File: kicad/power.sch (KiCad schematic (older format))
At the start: 30 parts, among them CON23 PS-ON, CON24 CON6, CON25 FAN, CON26 Chamber, Q7 FDC6401N, Q8 FDC6401N, Q9 FDC6401N

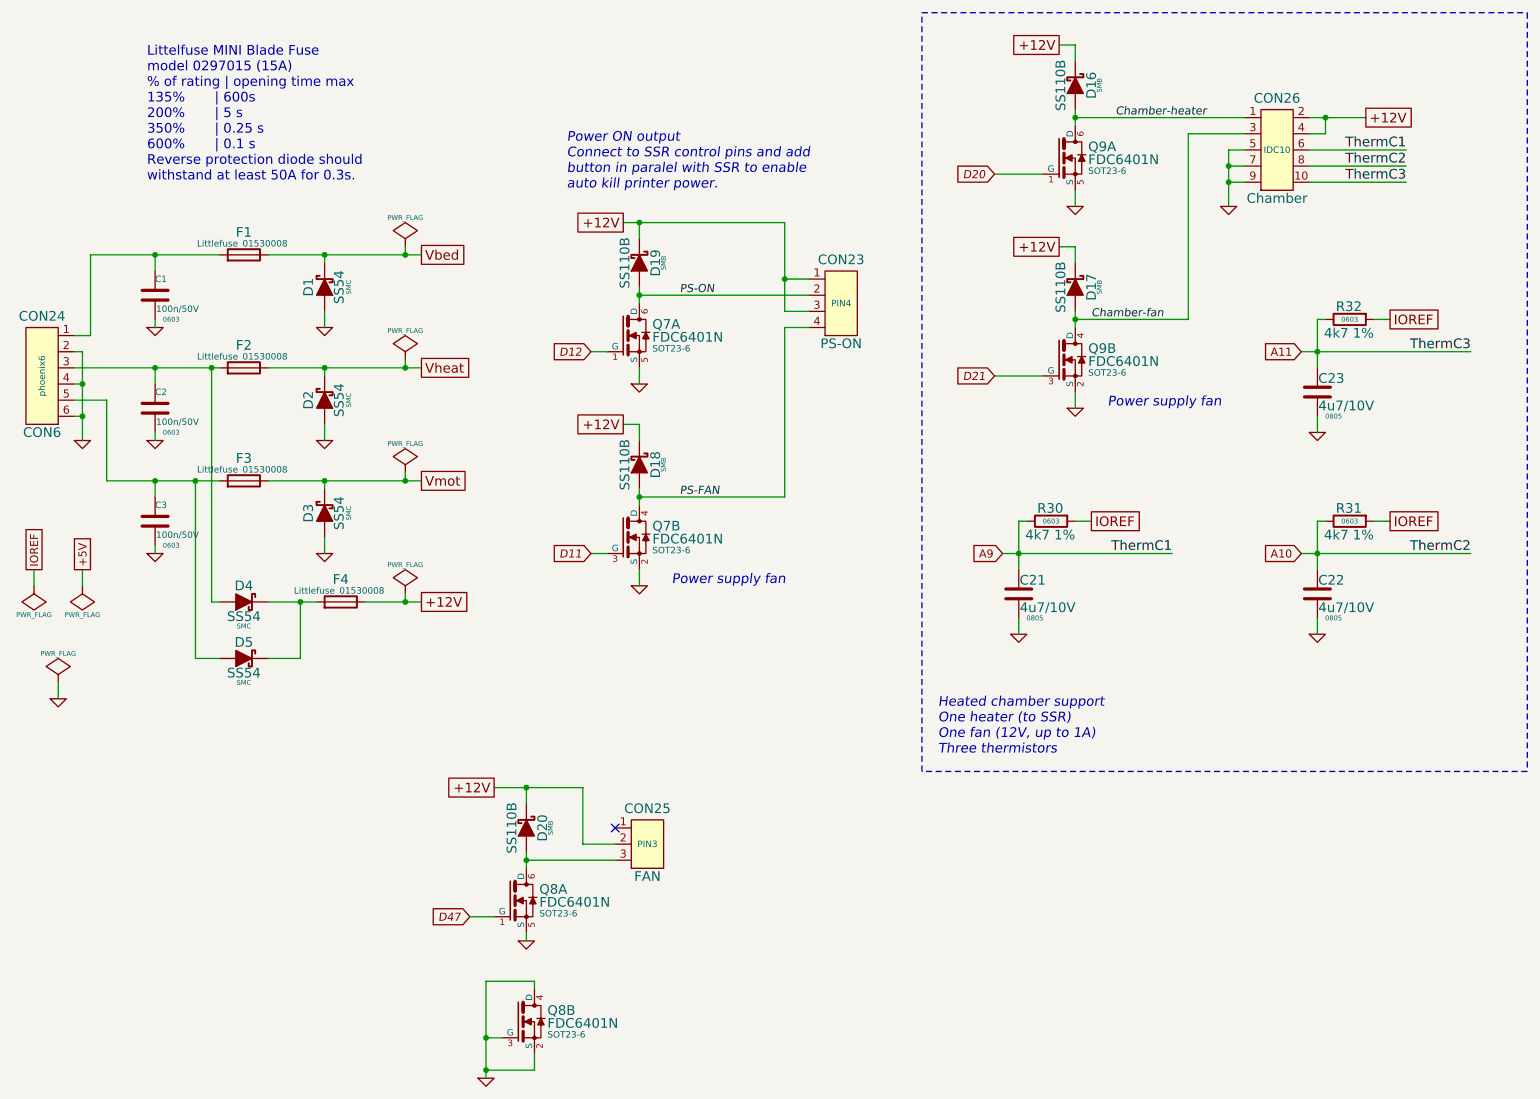
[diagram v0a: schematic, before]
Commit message: Change 1A diodes. Add capacitors next to OC outputs. Place.
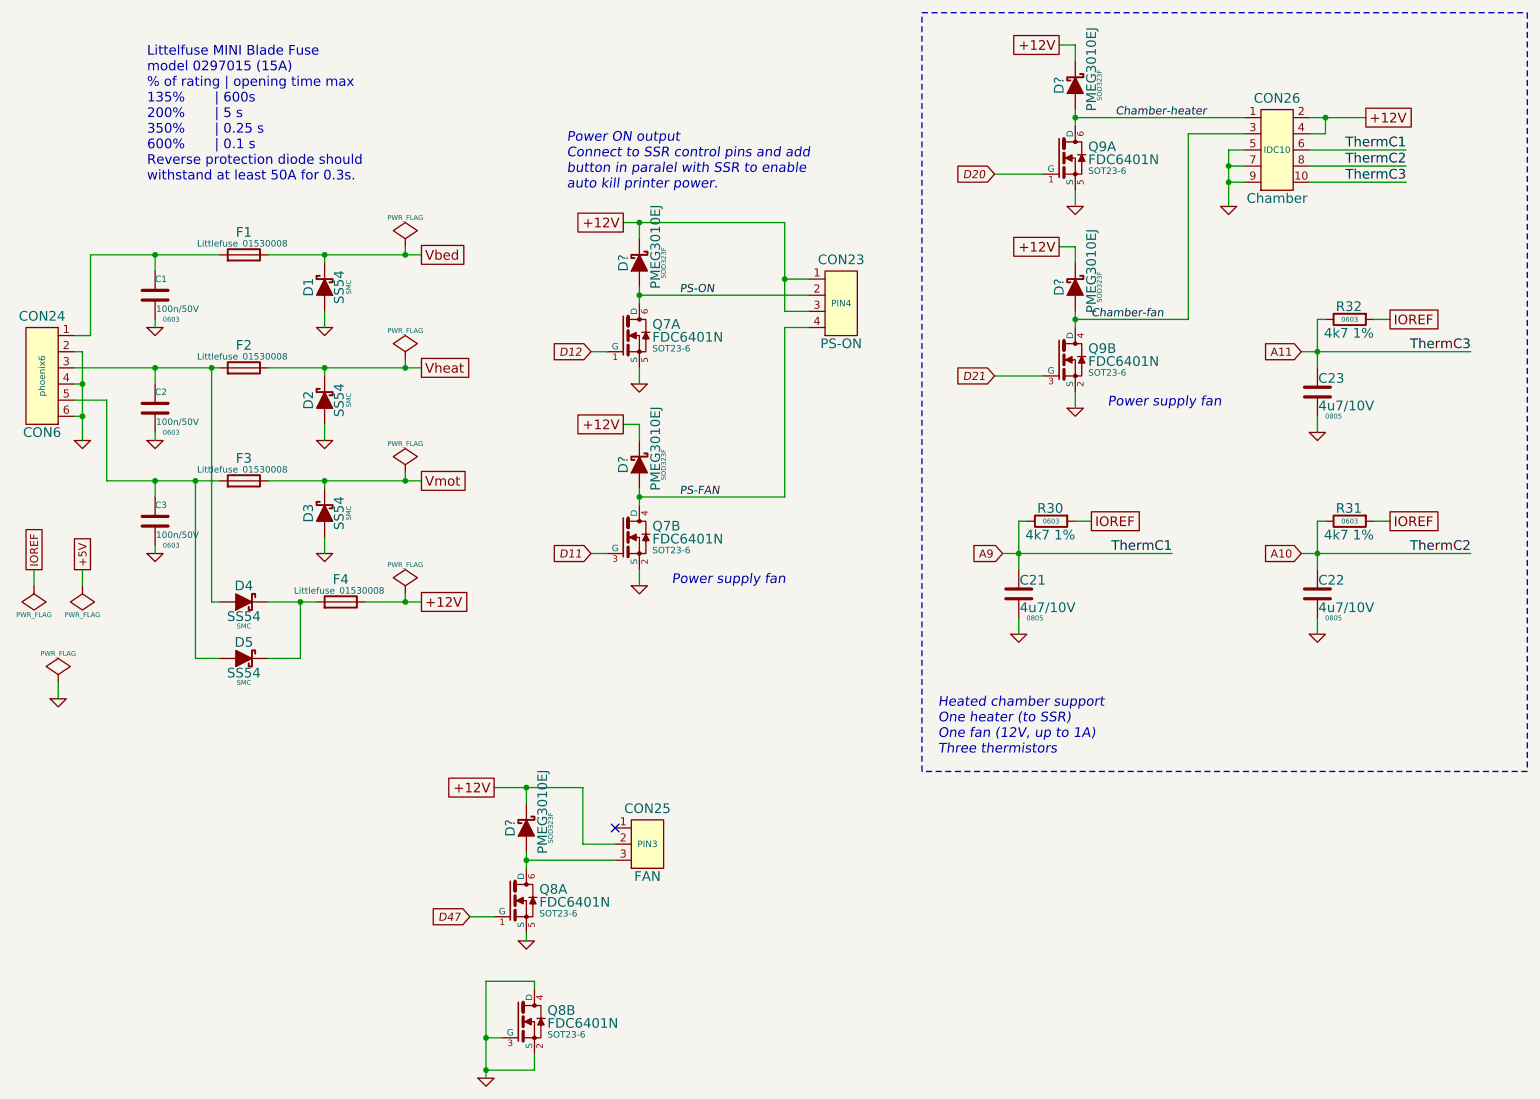
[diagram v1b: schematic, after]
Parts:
- removed D16, D17, D18, D19, D20: SS110B, SMB, symbol SS110B
- added D? (x5): PMEG3010EJ, SOD323F, symbol PMEG3010EJ
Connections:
- net +12V: now also D?.1, D?.1, D?.1, D?.1, D?.1
- net Chamber-fan: now also D?.2
- net Chamber-heater: now also D?.2
- net PS-FAN: now also D?.2
- net PS-ON: now also D?.2
- net at CON25.3, Q8.6 (D): now also D?.2
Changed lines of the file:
@@
 	1    0    0    -1
-$EndComp
-$Comp
-L SS110B D19
-U 1 1 53949E2B
-P 4850 2150
-F 0 "D19" H 4850 2050 60  0000 C CNN
-F 1 "SS110B" H 4850 2240 60  0000 C CNN
-F 2 "SMB" H 4850 2000 30  0000 C CNN
-F 3 "" V 4850 2150 60  0000 C CNN
-	1    4850 2150
-	0    -1   -1   0
 $EndComp
 Wire Wire Line
@@
 Heated chamber support\nOne heater (to SSR)\nOne fan (12V, up to 1A)\nThree thermistors
 $Comp
-L SS110B D18
-U 1 1 539B1F63
+L PMEG3010EJ D?
+U 1 1 539CBBDC
 P 4850 3400
-F 0 "D18" H 4850 3300 60  0000 C CNN
-F 1 "SS110B" H 4850 3490 60  0000 C CNN
-F 2 "SMB" H 4850 3250 30  0000 C CNN
+F 0 "D?" H 4850 3500 60  0000 C CNN
+F 1 "PMEG3010EJ" H 4950 3300 60  0000 C CNN
+F 2 "SOD323F" H 4850 3250 30  0000 C CNN
 F 3 "" V 4850 3400 60  0000 C CNN
 	1    4850 3400
@@
 $EndComp
 $Comp
-L SS110B D17
-U 1 1 539B1FBA
+L PMEG3010EJ D?
+U 1 1 539CBCF5
+P 4850 2150
+F 0 "D?" H 4850 2250 60  0000 C CNN
+F 1 "PMEG3010EJ" H 4950 2050 60  0000 C CNN
+F 2 "SOD323F" H 4850 2000 30  0000 C CNN
+F 3 "" V 4850 2150 60  0000 C CNN
+	1    4850 2150
+	0    -1   -1   0
+$EndComp
+$Comp
+L PMEG3010EJ D?
+U 1 1 539CBD53
+P 7550 1050
+F 0 "D?" H 7550 1150 60  0000 C CNN
+F 1 "PMEG3010EJ" H 7650 950 60  0000 C CNN
+F 2 "SOD323F" H 7550 900 30  0000 C CNN
+F 3 "" V 7550 1050 60  0000 C CNN
+	1    7550 1050
+	0    -1   -1   0
+$EndComp
+$Comp
+L PMEG3010EJ D?
+U 1 1 539CBDBC
 P 7550 2300
-F 0 "D17" H 7550 2200 60  0000 C CNN
-F 1 "SS110B" H 7550 2390 60  0000 C CNN
-F 2 "SMB" H 7550 2150 30  0000 C CNN
+F 0 "D?" H 7550 2400 60  0000 C CNN
+F 1 "PMEG3010EJ" H 7650 2200 60  0000 C CNN
+F 2 "SOD323F" H 7550 2150 30  0000 C CNN
 F 3 "" V 7550 2300 60  0000 C CNN
 	1    7550 2300
@@
 $EndComp
 $Comp
-L SS110B D16
-U 1 1 539B202A
-P 7550 1050
-F 0 "D16" H 7550 950 60  0000 C CNN
-F 1 "SS110B" H 7550 1140 60  0000 C CNN
-F 2 "SMB" H 7550 900 30  0000 C CNN
-F 3 "" V 7550 1050 60  0000 C CNN
-	1    7550 1050
-	0    -1   -1   0
-$EndComp
-$Comp
-L SS110B D20
-U 1 1 539B228F
+L PMEG3010EJ D?
+U 1 1 539CBE38
 P 4150 5650
-F 0 "D20" H 4150 5550 60  0000 C CNN
-F 1 "SS110B" H 4150 5740 60  0000 C CNN
-F 2 "SMB" H 4150 5500 30  0000 C CNN
+F 0 "D?" H 4150 5750 60  0000 C CNN
+F 1 "PMEG3010EJ" H 4250 5550 60  0000 C CNN
+F 2 "SOD323F" H 4150 5500 30  0000 C CNN
 F 3 "" V 4150 5650 60  0000 C CNN
 	1    4150 5650

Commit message: Place
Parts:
- added C27, C28, C29: 100n/50V, 0603, symbol C
- gave numbers to parts that had none: 5
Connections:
- net +12V: now also C27.1, C28.1, C29.1
- net GND: now also C27.2, C28.2, C29.2

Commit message: Fix panel connections. Place.
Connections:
- net D11: now also Q7.1 (G); no longer Q7.3 (G)
- net D12: now also Q7.3 (G); no longer Q7.1 (G)
- net PS-FAN: now also Q7.6 (D); no longer Q7.4 (D)
- net PS-ON: now also Q7.4 (D); no longer Q7.6 (D)
- net D20 renamed A3
- net D21 renamed A4
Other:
- moved on the sheet: Q7A, Q7B
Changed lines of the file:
@@
 $EndDescr
 $Comp
-L GND #PWR68
+L GND #PWR060
 U 1 1 53943822
 P 1400 3250
-F 0 "#PWR68" H 1400 3250 30  0001 C CNN
+F 0 "#PWR060" H 1400 3250 30  0001 C CNN
 F 1 "GND" H 1400 3180 30  0001 C CNN
 F 2 "" H 1400 3250 60  0000 C CNN
@@
 Littelfuse MINI Blade Fuse\nmodel 0297015 (15A)\n% of rating | opening time max\n135%       | 600s\n200%       | 5 s \n350%       | 0.25 s \n600%       | 0.1 s\nReverse protection diode should \nwithstand at least 50A for 0.3s.
 $Comp
-L GND #PWR70
+L GND #PWR061
 U 1 1 53943829
 P 2900 3250
-F 0 "#PWR70" H 2900 3250 30  0001 C CNN
+F 0 "#PWR061" H 2900 3250 30  0001 C CNN
 F 1 "GND" H 2900 3180 30  0001 C CNN
 F 2 "" H 2900 3250 60  0000 C CNN
@@
 $EndComp
 $Comp
-L GND #PWR64
+L GND #PWR062
 U 1 1 5394382F
 P 2900 2550
-F 0 "#PWR64" H 2900 2550 30  0001 C CNN
+F 0 "#PWR062" H 2900 2550 30  0001 C CNN
 F 1 "GND" H 2900 2480 30  0001 C CNN
 F 2 "" H 2900 2550 60  0000 C CNN
@@
 $EndComp
 $Comp
-L GND #PWR73
+L GND #PWR063
 U 1 1 53943835
 P 2900 3950
-F 0 "#PWR73" H 2900 3950 30  0001 C CNN
+F 0 "#PWR063" H 2900 3950 30  0001 C CNN
 F 1 "GND" H 2900 3880 30  0001 C CNN
 F 2 "" H 2900 3950 60  0000 C CNN
@@
 $EndComp
 $Comp
-L GND #PWR63
+L GND #PWR064
 U 1 1 53943842
 P 1850 2550
-F 0 "#PWR63" H 1850 2550 30  0001 C CNN
+F 0 "#PWR064" H 1850 2550 30  0001 C CNN
 F 1 "GND" H 1850 2480 30  0001 C CNN
 F 2 "" H 1850 2550 60  0000 C CNN
@@
 $EndComp
 $Comp
-L GND #PWR69
+L GND #PWR065
 U 1 1 53943848
 P 1850 3250
-F 0 "#PWR69" H 1850 3250 30  0001 C CNN
+F 0 "#PWR065" H 1850 3250 30  0001 C CNN
 F 1 "GND" H 1850 3180 30  0001 C CNN
 F 2 "" H 1850 3250 60  0000 C CNN
@@
 $EndComp
 $Comp
-L GND #PWR72
+L GND #PWR066
 U 1 1 5394384E
 P 1850 3950
-F 0 "#PWR72" H 1850 3950 30  0001 C CNN
+F 0 "#PWR066" H 1850 3950 30  0001 C CNN
 F 1 "GND" H 1850 3880 30  0001 C CNN
 F 2 "" H 1850 3950 60  0000 C CNN
@@
 $EndComp
 $Comp
-L PWR_FLAG #FLG1
+L PWR_FLAG #FLG067
 U 1 1 539438AC
 P 3400 2050
-F 0 "#FLG1" H 3400 2145 30  0001 C CNN
+F 0 "#FLG067" H 3400 2145 30  0001 C CNN
 F 1 "PWR_FLAG" H 3400 2230 30  0000 C CNN
 F 2 "" H 3400 2050 60  0000 C CNN
@@
 $EndComp
 $Comp
-L PWR_FLAG #FLG2
+L PWR_FLAG #FLG068
 U 1 1 539438B2
 P 3400 2750
-F 0 "#FLG2" H 3400 2845 30  0001 C CNN
+F 0 "#FLG068" H 3400 2845 30  0001 C CNN
 F 1 "PWR_FLAG" H 3400 2930 30  0000 C CNN
 F 2 "" H 3400 2750 60  0000 C CNN
@@
 $EndComp
 $Comp
-L PWR_FLAG #FLG3
+L PWR_FLAG #FLG069
 U 1 1 539438B8
 P 3400 3450
-F 0 "#FLG3" H 3400 3545 30  0001 C CNN
+F 0 "#FLG069" H 3400 3545 30  0001 C CNN
 F 1 "PWR_FLAG" H 3400 3630 30  0000 C CNN
 F 2 "" H 3400 3450 60  0000 C CNN
@@
 $EndComp
 $Comp
-L PWR_FLAG #FLG6
+L PWR_FLAG #FLG070
 U 1 1 539438BE
 P 3400 4200
-F 0 "#FLG6" H 3400 4295 30  0001 C CNN
+F 0 "#FLG070" H 3400 4295 30  0001 C CNN
 F 1 "PWR_FLAG" H 3400 4380 30  0000 C CNN
 F 2 "" H 3400 4200 60  0000 C CNN
@@
 $EndComp
 $Comp
-L PWR_FLAG #FLG7
+L PWR_FLAG #FLG071
 U 1 1 539438C4
 P 1250 4750
-F 0 "#FLG7" H 1250 4845 30  0001 C CNN
+F 0 "#FLG071" H 1250 4845 30  0001 C CNN
 F 1 "PWR_FLAG" H 1250 4930 30  0000 C CNN
 F 2 "" H 1250 4750 60  0000 C CNN
@@
 $EndComp
 $Comp
-L GND #PWR77
+L GND #PWR072
 U 1 1 539438CA
 P 1250 4850
-F 0 "#PWR77" H 1250 4850 30  0001 C CNN
+F 0 "#PWR072" H 1250 4850 30  0001 C CNN
 F 1 "GND" H 1250 4780 30  0001 C CNN
 F 2 "" H 1250 4850 60  0000 C CNN
@@
 IOREF
 $Comp
-L PWR_FLAG #FLG5
+L PWR_FLAG #FLG073
 U 1 1 53943908
 P 1400 4150
-F 0 "#FLG5" H 1400 4245 30  0001 C CNN
+F 0 "#FLG073" H 1400 4245 30  0001 C CNN
 F 1 "PWR_FLAG" H 1400 4330 30  0000 C CNN
 F 2 "" H 1400 4150 60  0000 C CNN
@@
 $EndComp
 $Comp
-L PWR_FLAG #FLG4
+L PWR_FLAG #FLG074
 U 1 1 5394390F
 P 1100 4150
-F 0 "#FLG4" H 1100 4245 30  0001 C CNN
+F 0 "#FLG074" H 1100 4245 30  0001 C CNN
 F 1 "PWR_FLAG" H 1100 4330 30  0000 C CNN
 F 2 "" H 1100 4150 60  0000 C CNN
@@
 L FDC6401N Q7
 U 1 1 5394391D
+P 4750 3850
+F 0 "Q7" H 4930 3920 60  0000 L CNN
+F 1 "FDC6401N" H 4930 3840 60  0000 L CNN
+F 2 "SOT23-6" H 4930 3770 40  0000 L CNN
+F 3 "" H 4750 3800 60  0000 C CNN
+	1    4750 3850
+	1    0    0    -1
+$EndComp
+$Comp
+L FDC6401N Q7
+U 2 1 53943924
 P 4750 2600
 F 0 "Q7" H 4930 2670 60  0000 L CNN
@@
 F 2 "SOT23-6" H 4930 2520 40  0000 L CNN
 F 3 "" H 4750 2550 60  0000 C CNN
-	1    4750 2600
-	1    0    0    -1
-$EndComp
-$Comp
-L FDC6401N Q7
-U 2 1 53943924
-P 4750 3850
-F 0 "Q7" H 4930 3920 60  0000 L CNN
-F 1 "FDC6401N" H 4930 3840 60  0000 L CNN
-F 2 "SOT23-6" H 4930 3770 40  0000 L CNN
-F 3 "" H 4750 3800 60  0000 C CNN
-	2    4750 3850
-	1    0    0    -1
-$EndComp
-$Comp
-L GND #PWR74
+	2    4750 2600
+	1    0    0    -1
+$EndComp
+$Comp
+L GND #PWR075
 U 1 1 53943ED6
 P 4850 4150
-F 0 "#PWR74" H 4850 4150 30  0001 C CNN
+F 0 "#PWR075" H 4850 4150 30  0001 C CNN
 F 1 "GND" H 4850 4080 30  0001 C CNN
 F 2 "" H 4850 4150 60  0000 C CNN
@@
 $EndComp
 $Comp
-L GND #PWR65
+L GND #PWR076
 U 1 1 53943F43
 P 4850 2900
-F 0 "#PWR65" H 4850 2900 30  0001 C CNN
+F 0 "#PWR076" H 4850 2900 30  0001 C CNN
 F 1 "GND" H 4850 2830 30  0001 C CNN
 F 2 "" H 4850 2900 60  0000 C CNN
@@
 D47
 $Comp
-L GND #PWR79
+L GND #PWR077
 U 1 1 53948CCE
 P 4150 6350
-F 0 "#PWR79" H 4150 6350 30  0001 C CNN
+F 0 "#PWR077" H 4150 6350 30  0001 C CNN
 F 1 "GND" H 4150 6280 30  0001 C CNN
 F 2 "" H 4150 6350 60  0000 C CNN
@@
 Connection ~ 3900 7150
 $Comp
-L GND #PWR80
+L GND #PWR078
 U 1 1 53949810
 P 3900 7200
-F 0 "#PWR80" H 3900 7200 30  0001 C CNN
+F 0 "#PWR078" H 3900 7200 30  0001 C CNN
 F 1 "GND" H 3900 7130 30  0001 C CNN
 F 2 "" H 3900 7200 60  0000 C CNN
@@
 $EndComp
 $Comp
-L GND #PWR66
+L GND #PWR079
 U 1 1 5394A1DE
 P 7550 3050
-F 0 "#PWR66" H 7550 3050 30  0001 C CNN
+F 0 "#PWR079" H 7550 3050 30  0001 C CNN
 F 1 "GND" H 7550 2980 30  0001 C CNN
 F 2 "" H 7550 3050 60  0000 C CNN
@@
 $EndComp
 $Comp
-L GND #PWR61
+L GND #PWR080
 U 1 1 5394A1E4
 P 7550 1800
-F 0 "#PWR61" H 7550 1800 30  0001 C CNN
+F 0 "#PWR080" H 7550 1800 30  0001 C CNN
 F 1 "GND" H 7550 1730 30  0001 C CNN
 F 2 "" H 7550 1800 60  0000 C CNN
@@
 +12V
 Text GLabel 7050 1600 0    50   Input Italic 0
-D20
+A3
 Wire Wire Line
 	7550 1200 7550 1300
@@
 	7350 2850 7050 2850
 Text GLabel 7050 2850 0    50   Input Italic 0
-D21
+A4
 Text Notes 7750 3050 0    60   Italic 0
 Power supply fan
@@
 Connection ~ 8500 1550
 $Comp
-L GND #PWR62
+L GND #PWR081
 U 1 1 5394B08E
 P 8500 1800
-F 0 "#PWR62" H 8500 1800 30  0001 C CNN
+F 0 "#PWR081" H 8500 1800 30  0001 C CNN
 F 1 "GND" H 8500 1730 30  0001 C CNN
 F 2 "" H 8500 1800 60  0000 C CNN
@@
 $EndComp
 $Comp
-L GND #PWR75
+L GND #PWR082
 U 1 1 5394B617
 P 7200 4450
-F 0 "#PWR75" H 7200 4450 30  0001 C CNN
+F 0 "#PWR082" H 7200 4450 30  0001 C CNN
 F 1 "GND" H 7200 4380 30  0001 C CNN
 F 2 "~" H 7200 4450 60  0000 C CNN
@@
 $EndComp
 $Comp
-L GND #PWR76
+L GND #PWR083
 U 1 1 5394B93D
 P 9050 4450
-F 0 "#PWR76" H 9050 4450 30  0001 C CNN
+F 0 "#PWR083" H 9050 4450 30  0001 C CNN
 F 1 "GND" H 9050 4380 30  0001 C CNN
 F 2 "~" H 9050 4450 60  0000 C CNN
@@
 $EndComp
 $Comp
-L GND #PWR67
+L GND #PWR084
 U 1 1 5394BA08
 P 9050 3200
-F 0 "#PWR67" H 9050 3200 30  0001 C CNN
+F 0 "#PWR084" H 9050 3200 30  0001 C CNN
 F 1 "GND" H 9050 3130 30  0001 C CNN
 F 2 "~" H 9050 3200 60  0000 C CNN
@@
 $EndComp
 $Comp
-L GND #PWR78
+L GND #PWR085
 U 1 1 539CFAEC
 P 3850 5850
-F 0 "#PWR78" H 3850 5850 30  0001 C CNN
+F 0 "#PWR085" H 3850 5850 30  0001 C CNN
 F 1 "GND" H 3850 5780 30  0001 C CNN
 F 2 "" H 3850 5850 60  0000 C CNN
@@
 $EndComp
 $Comp
-L GND #PWR71
+L GND #PWR086
 U 1 1 539CFEC7
 P 4500 3600
-F 0 "#PWR71" H 4500 3600 30  0001 C CNN
+F 0 "#PWR086" H 4500 3600 30  0001 C CNN
 F 1 "GND" H 4500 3530 30  0001 C CNN
 F 2 "" H 4500 3600 60  0000 C CNN
@@
 Connection ~ 7250 800
 $Comp
-L GND #PWR60
+L GND #PWR087
 U 1 1 539D0988
 P 7250 1250
-F 0 "#PWR60" H 7250 1250 30  0001 C CNN
+F 0 "#PWR087" H 7250 1250 30  0001 C CNN
 F 1 "GND" H 7250 1180 30  0001 C CNN
 F 2 "" H 7250 1250 60  0000 C CNN

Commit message: Delete fuse on +12V. Chcange fuse & diode placement.
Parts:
- removed F4: MINI_Blade_Fuse_Holder, Littlefuse_01530008, symbol MINI_Blade_Fuse_Holder
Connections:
- net +12V: now also D4.1, D5.1
- net Vheat: now also D4.2
- net Vmot: now also D5.2
- net at C2.1, CON24.3, F2.1: no longer D4.2
- net at C3.1, CON24.5, F3.1: no longer D5.2
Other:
- moved on the sheet: D4, D5, F2, F3
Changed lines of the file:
@@
 L SS54 D4
 U 1 1 5394387A
-P 2400 4250
-F 0 "D4" H 2400 4150 60  0000 C CNN
-F 1 "SS54" H 2400 4340 60  0000 C CNN
-F 2 "SMC" H 2400 4400 30  0000 C CNN
-F 3 "" V 2400 4250 60  0000 C CNN
-	1    2400 4250
+P 2900 4250
+F 0 "D4" H 2900 4150 60  0000 C CNN
+F 1 "SS54" H 2900 4340 60  0000 C CNN
+F 2 "SMC" H 2900 4400 30  0000 C CNN
+F 3 "" V 2900 4250 60  0000 C CNN
+	1    2900 4250
 	1    0    0    1
 $EndComp
@@
 L SS54 D5
 U 1 1 53943881
-P 2400 4600
-F 0 "D5" H 2400 4500 60  0000 C CNN
-F 1 "SS54" H 2400 4690 60  0000 C CNN
-F 2 "SMC" H 2400 4750 30  0000 C CNN
-F 3 "" V 2400 4600 60  0000 C CNN
-	1    2400 4600
+P 2900 4600
+F 0 "D5" H 2900 4500 60  0000 C CNN
+F 1 "SS54" H 2900 4690 60  0000 C CNN
+F 2 "SMC" H 2900 4750 30  0000 C CNN
+F 3 "" V 2900 4600 60  0000 C CNN
+	1    2900 4600
 	1    0    0    1
 $EndComp
@@
 L MINI_Blade_Fuse_Holder F2
 U 1 1 5394388F
-P 2400 2800
-F 0 "F2" H 2400 2940 60  0000 C CNN
-F 1 "MINI_Blade_Fuse_Holder" H 2400 2715 60  0001 C CNN
-F 2 "Littlefuse_01530008" H 2390 2870 40  0000 C CNN
-F 3 "" V 2400 2800 30  0000 C CNN
-	1    2400 2800
+P 2300 2800
+F 0 "F2" H 2300 2940 60  0000 C CNN
+F 1 "MINI_Blade_Fuse_Holder" H 2300 2715 60  0001 C CNN
+F 2 "Littlefuse_01530008" H 2290 2870 40  0000 C CNN
+F 3 "" V 2300 2800 30  0000 C CNN
+	1    2300 2800
 	1    0    0    -1
 $EndComp
@@
 L MINI_Blade_Fuse_Holder F3
 U 1 1 53943896
-P 2400 3500
-F 0 "F3" H 2400 3640 60  0000 C CNN
-F 1 "MINI_Blade_Fuse_Holder" H 2400 3415 60  0001 C CNN
-F 2 "Littlefuse_01530008" H 2390 3570 40  0000 C CNN
-F 3 "" V 2400 3500 30  0000 C CNN
-	1    2400 3500
-	1    0    0    -1
-$EndComp
-$Comp
-L MINI_Blade_Fuse_Holder F4
-U 1 1 5394389D
-P 3000 4250
-F 0 "F4" H 3000 4390 60  0000 C CNN
-F 1 "MINI_Blade_Fuse_Holder" H 3000 4165 60  0001 C CNN
-F 2 "Littlefuse_01530008" H 2990 4320 40  0000 C CNN
-F 3 "" V 3000 4250 30  0000 C CNN
-	1    3000 4250
+P 2300 3500
+F 0 "F3" H 2300 3640 60  0000 C CNN
+F 1 "MINI_Blade_Fuse_Holder" H 2300 3415 60  0001 C CNN
+F 2 "Littlefuse_01530008" H 2290 3570 40  0000 C CNN
+F 3 "" V 2300 3500 30  0000 C CNN
+	1    2300 3500
 	1    0    0    -1
 $EndComp
@@
 Connection ~ 3400 4250
 Wire Wire Line
-	3400 4200 3400 4250
+	3400 4250 3400 4200
 Wire Wire Line
 	2900 3250 2900 3150
@@
 Connection ~ 2900 2100
 Connection ~ 2900 2800
-Wire Wire Line
-	3150 4250 3500 4250
 Connection ~ 2900 3500
 Connection ~ 1400 3100
@@
 Wire Wire Line
 	1850 3500 1850 3600
-Connection ~ 2100 3500
-Wire Wire Line
-	2100 3500 2100 4600
-Connection ~ 2750 4250
-Wire Wire Line
-	2750 4600 2750 4250
-Wire Wire Line
-	2550 4600 2750 4600
-Wire Wire Line
-	2550 4250 2850 4250
-Wire Wire Line
-	2100 4600 2250 4600
-Connection ~ 2200 2800
-Wire Wire Line
-	2200 4250 2250 4250
-Wire Wire Line
-	2200 2800 2200 4250
+Connection ~ 3150 4250
+Wire Wire Line
+	3150 4600 3150 4250
+Wire Wire Line
+	3050 4600 3150 4600
+Wire Wire Line
+	2500 4600 2750 4600
+Wire Wire Line
+	2650 4250 2750 4250
 Wire Wire Line
 	2900 3500 2900 3550
 Wire Wire Line
-	2550 3500 3500 3500
+	2450 3500 3500 3500
 Wire Wire Line
 	2900 2100 2900 2150
@@
 	2900 2800 2900 2850
 Wire Wire Line
-	2550 2800 3500 2800
+	2450 2800 3500 2800
 Wire Wire Line
 	1450 2100 2250 2100
 Wire Wire Line
-	1550 3500 2250 3500
+	1550 3500 2150 3500
 Wire Wire Line
 	1550 3000 1550 3500
@@
 	1450 2600 1350 2600
 Wire Wire Line
-	1350 2800 2250 2800
+	1350 2800 2150 2800
 Connection ~ 1400 2900
 Wire Wire Line
@@
 Chamber-fan
 Wire Wire Line
-	7550 900  7550 800
+	7550 800  7550 900
 Connection ~ 7550 1250
 Wire Wire Line
-	7550 800  7100 800
+	7100 800  7550 800
 Text GLabel 9350 1250 2    60   UnSpc ~ 0
 +12V
@@
 Wire Wire Line
 	7250 1250 7250 1200
+Wire Wire Line
+	3050 4250 3500 4250
+Wire Wire Line
+	2500 4600 2500 3500
+Connection ~ 2500 3500
+Wire Wire Line
+	2650 4250 2650 2800
+Connection ~ 2650 2800
 $EndSCHEMATC
